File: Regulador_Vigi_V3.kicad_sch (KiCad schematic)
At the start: 15 parts, among them J1 IN, J2 Out, U1 LM5163

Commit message: Se terminó el esquemático, Se añadió un capacitor adicional y se cambió el código del inductor
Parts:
- removed J1: IN, 1-Terminal-Block:AK700-DG129-1x02_P5.00mm, symbol 1-Terminal-Block:AK700-DG129-1x02_P5.00mm
- added C6: 100nF 50V, 1-Capacitor:C_0805_2012Metric, symbol 1-Capacitor:C_0805
- added D1: M7, 1-Diode:D_SMA, symbol 1-Diode:M7
- added D2: SMB39CA, Diode_SMD:D_SMB, symbol 1-Diode:SMB39CA
- added PAD1, PAD2, PAD3, PAD4, PAD5, PAD6: PAD_2.54_1.0, 1-Pad:PAD_2.54_1.0, symbol 1-Pad:PAD_2.54_1.0
- L1: value SMDRI127-331MT -> SMDRI127-101MT
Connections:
- net GND: now also C6.2, D2.2 (A2), PAD2.1, PAD4.1
- net VCC: now also C6.1, D1.1 (K)
- new net +VIN: D1.2 (A), D2.1 (A1), PAD1.1
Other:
- note added: "Adapter"
- note added: "C10150"
- note added: "C49678"
- note removed: "Buck Converter V1"
- note removed: "C10152"
- moved on the sheet: C1, C2, C3, C4, C5, J2, L1, R1, R2, R3, R4, TP1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

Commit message: SCH: Se cambiaron las resistencias del feedback, se limpiaron los comentarios. PCB: Se terminó de rutear. GITIGNORE: se agregó una línea
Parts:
- removed D1: M7, 1-Diode:D_SMA, symbol 1-Diode:M7
- removed D2: SMB39CA, Diode_SMD:D_SMB, symbol 1-Diode:SMB39CA
- removed J2: Out, 1-Terminal-Block:AK700-DG129-1x02_P5.00mm, symbol 1-Terminal-Block:AK700-DG129-1x02_P5.00mm
- removed TP1: VFB, TestPoint:TestPoint_Pad_D1.0mm, symbol Connector:TestPoint
- removed TP2: SW, TestPoint:TestPoint_Pad_D1.0mm, symbol Connector:TestPoint
- added C7: 100nF 50V, 1-Capacitor:C_0805_2012Metric, symbol 1-Capacitor:C_0805
- L1: value SMDRI127-101MT -> 100uH 1A; footprint 1-Inductor:DR127 -> 1-Inductor:L_8x8mm
- R3: value 698k -> 210k
- R4: value 49.9k -> 15k
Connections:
- net +5V is gone; now on net VOUT: C3.1, C5.1, L1.2, R3.1
- net +VIN is gone; now on net VCC: PAD1.1
- net GND: now also C7.2
- net VOUT: now reaches PAD3.1
- net VOUT: now also C7.1
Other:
- note added: "C17475"
- note added: "C218423"
- note added: "C341083"
- note removed: "C10150"
- note removed: "C23184"
- note removed: "C5126055"
- note removed: "Fsw (khz) = 5*2500/43 = 290.7kHz"
- note removed: "Inductor 330uH 1.1A https://www.tme.com/pe/es/details/srr1280-331k/chokes-smd-de-potencia/bourns/"
- moved on the sheet: C5, PAD1, PAD2, PAD3, PAD4, PAD5, PAD6

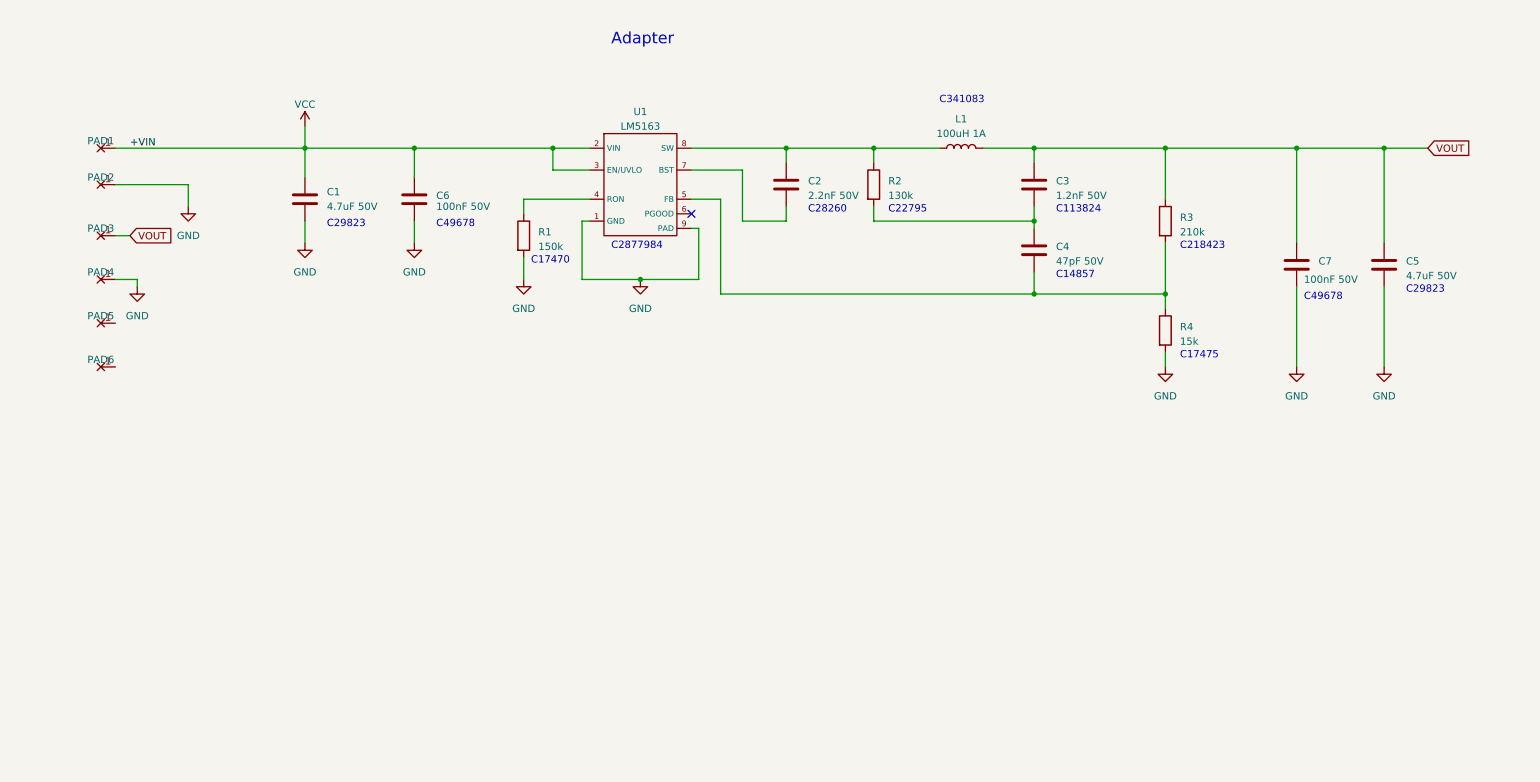
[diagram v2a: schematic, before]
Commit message: SCH:Se cambió comentarios de dos capacitores iniciales para soportar mayor voltaje. PCB:Se actualiza la PCB. JLCPCB:Se cambia el código del part de los capacitores
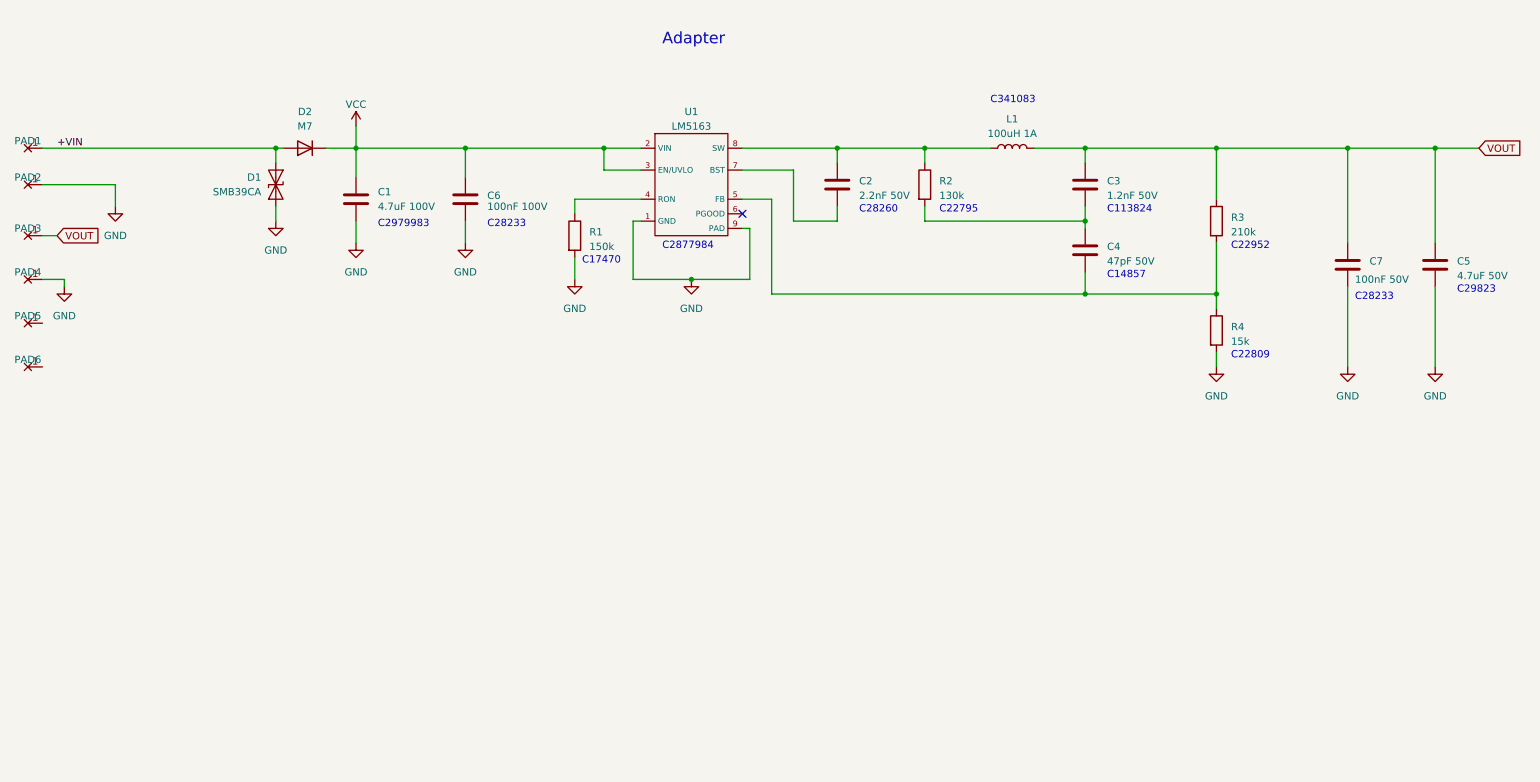
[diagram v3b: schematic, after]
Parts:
- added D1: SMB39CA, Diode_SMD:D_SMB, symbol 1-Diode:SMB39CA
- added D2: M7, 1-Diode:D_SMA, symbol 1-Diode:M7
- C1: value 4.7uF 50V -> 4.7uF 100V; footprint 1-Capacitor:C_1206_3216Metric -> 1-Capacitor:C_1210_3225Metric_Mod
- C6: value 100nF 50V -> 100nF 100V
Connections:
- net GND: now also D1.2 (A2)
- net VCC: now also D2.1 (K); no longer PAD1.1
- new net +VIN: D1.1 (A1), D2.2 (A), PAD1.1
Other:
- note added: "C22809"
- note added: "C22952"
- note added: "C28233"
- note added: "C2979983"
- note removed: "C17475"
- note removed: "C218423"
- note removed: "C49678"
- moved on the sheet: C1, C2, C3, C4, C5, C6, C7, L1, PAD1, PAD2, PAD3, PAD4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
